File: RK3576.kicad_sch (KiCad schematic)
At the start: 0 parts

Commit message: Add files via upload
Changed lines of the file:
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@@
+		)
+	)
+	(bus
+		(pts
+			(xy 0.1524 0.1524) (xy 53.4924 0.1524)
+		)
+		(stroke
+			(width 0)
+			(type default)
 		)
 	)

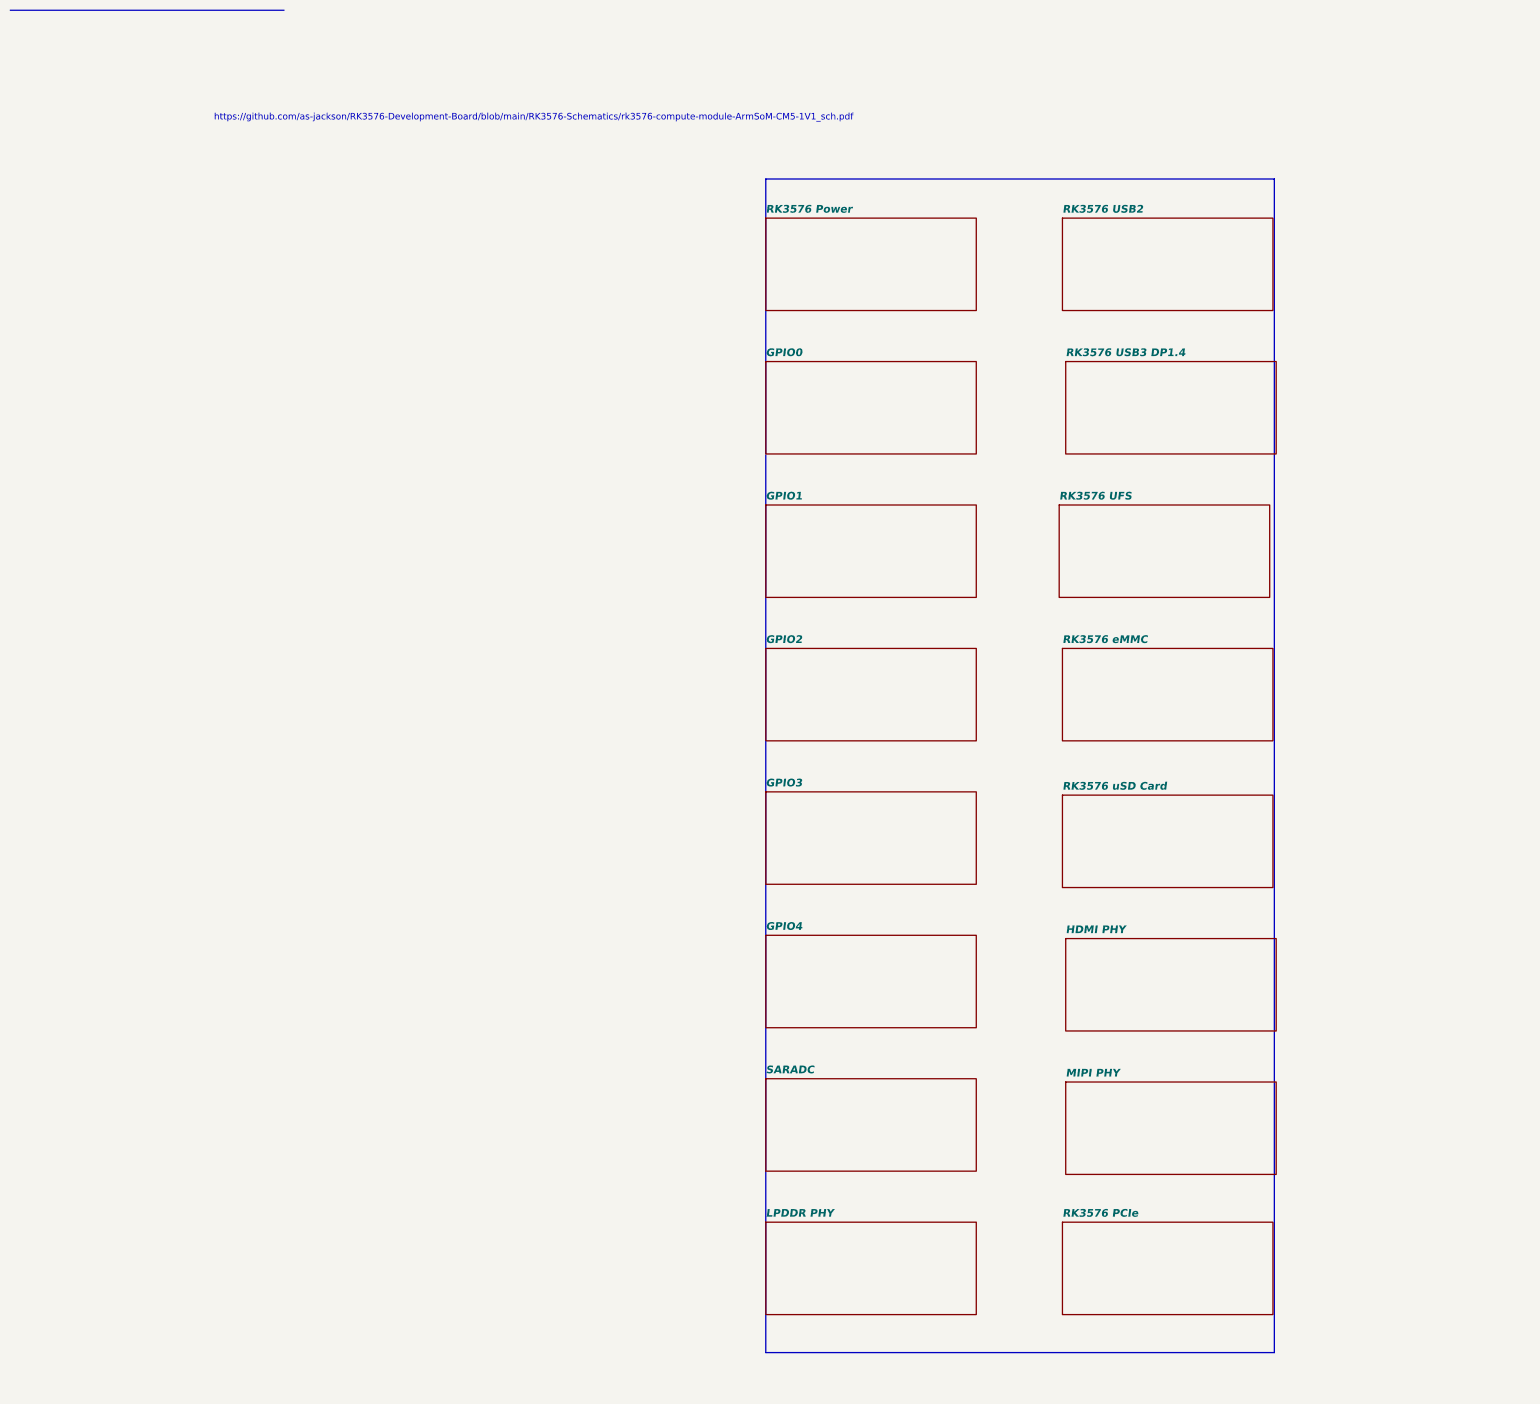
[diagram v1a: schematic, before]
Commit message: SBC Board V0.2
The SBC schematics before footprint and part number check
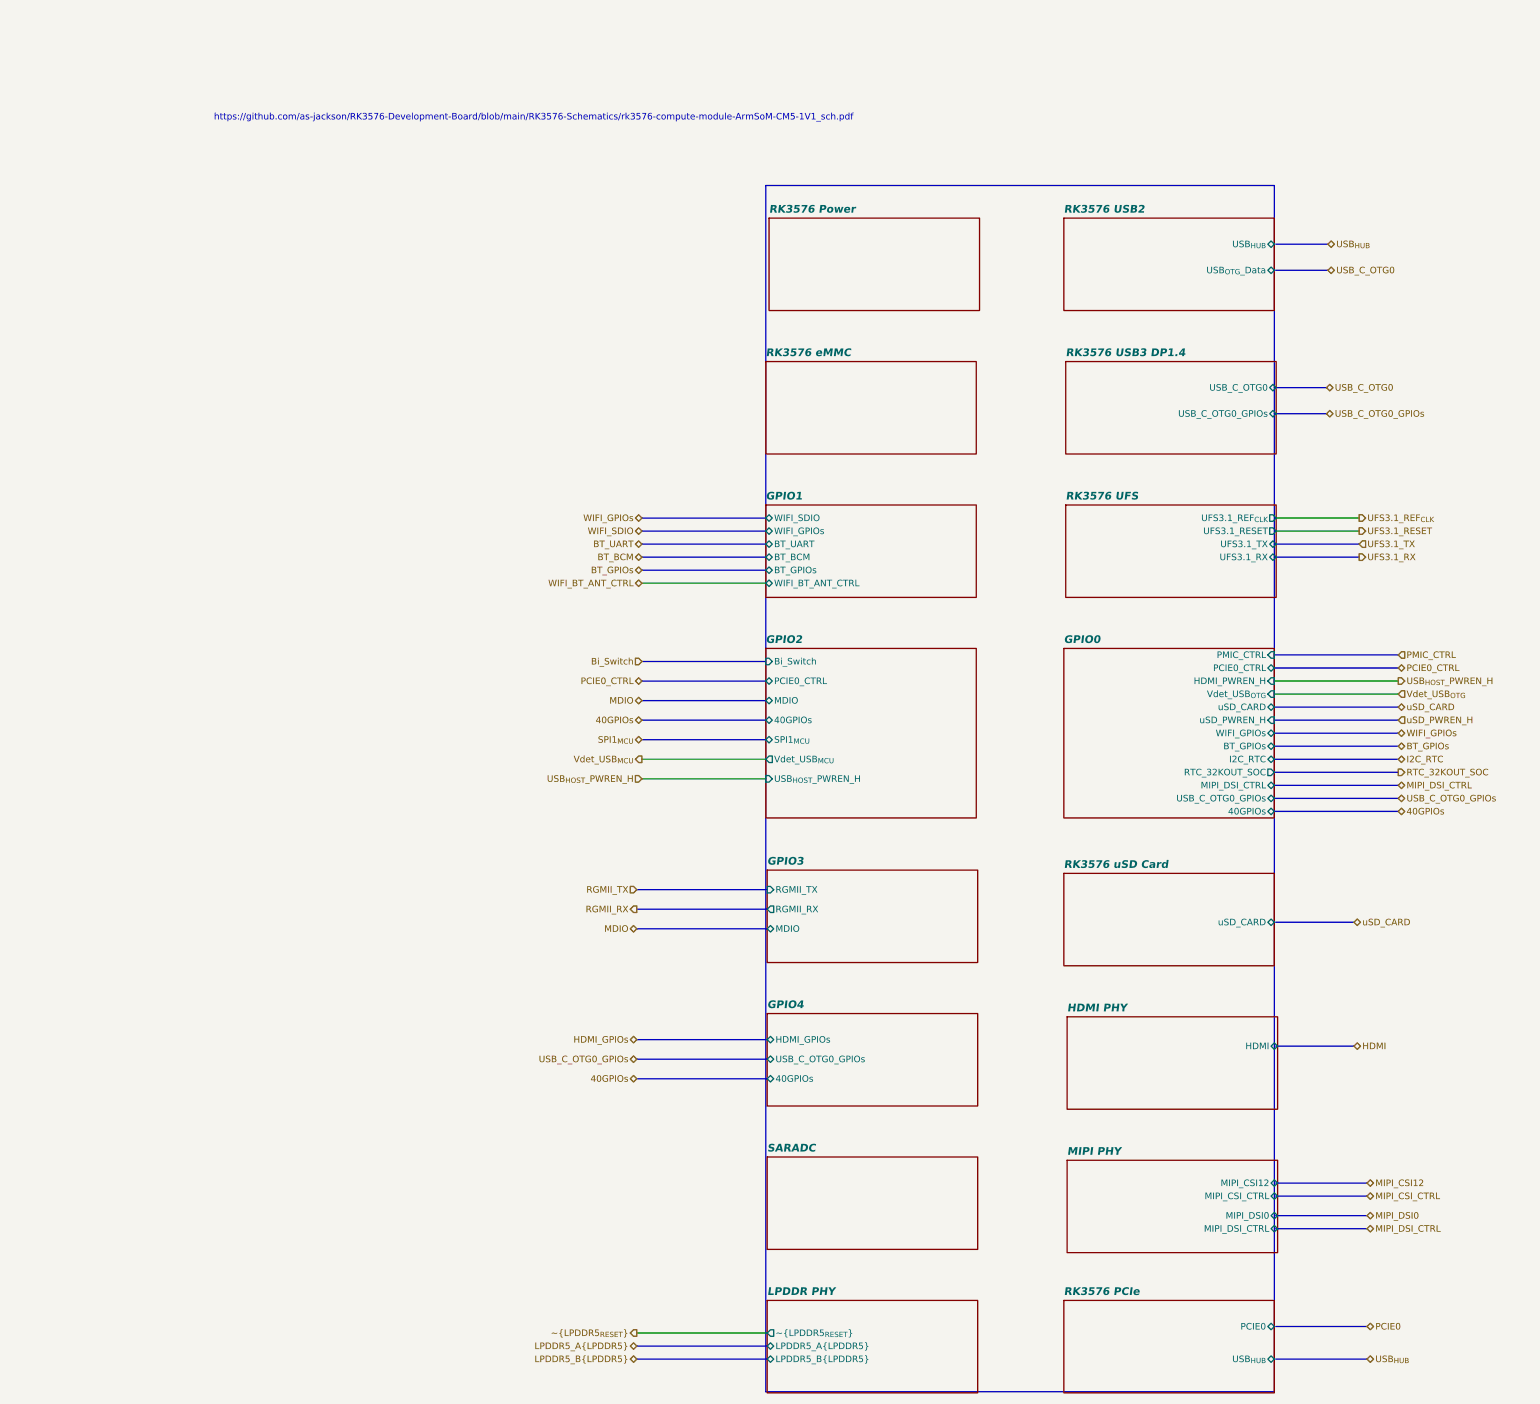
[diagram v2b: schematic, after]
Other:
- sheet GPIO0 ports: added 40GPIOs, BT_GPIOs, HDMI_PWREN_H, I2C_RTC, MIPI_DSI_CTRL, PCIE0_CTRL, PMIC_CTRL, RTC_32KOUT_SOC, USB_C_OTG0_GPIOs, Vdet_USB_{OTG}, WIFI_GPIOs, uSD_CARD, uSD_PWREN_H; removed none
- sheet GPIO1 ports: added BT_BCM, BT_GPIOs, BT_UART, WIFI_BT_ANT_CTRL, WIFI_GPIOs, WIFI_SDIO; removed none
- sheet GPIO2 ports: added 40GPIOs, Bi_Switch, MDIO, PCIE0_CTRL, SPI1_{MCU}, USB_{HOST}_PWREN_H, Vdet_USB_{MCU}; removed none
- sheet GPIO3 ports: added MDIO, RGMII_RX, RGMII_TX; removed none
- sheet GPIO4 ports: added 40GPIOs, HDMI_GPIOs, USB_C_OTG0_GPIOs; removed none
- sheet HDMI PHY ports: added HDMI; removed none
- sheet LPDDR PHY ports: added LPDDR5_A{LPDDR5}, LPDDR5_B{LPDDR5}, ~{LPDDR5_{RESET}}; removed none
- sheet MIPI PHY ports: added MIPI_CSI12, MIPI_CSI_CTRL, MIPI_DSI0, MIPI_DSI_CTRL; removed none
- sheet RK3576 PCIe ports: added PCIE0, USB_{HUB}; removed none
- sheet RK3576 UFS ports: added UFS3.1_REF_{CLK}, UFS3.1_RESET, UFS3.1_RX, UFS3.1_TX; removed none
- sheet RK3576 USB2 ports: added USB_{HUB}, USB_{OTG}_Data; removed none
- sheet RK3576 USB3 DP1.4 ports: added USB_C_OTG0, USB_C_OTG0_GPIOs; removed none
- sheet RK3576 uSD Card ports: added uSD_CARD; removed none

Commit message: Release v2: replace main with RK3576 SBCv2, archive v1 to branch archive/v1
- main now shows only v2 (RK3576 SBCv2.kicad_pro)
- v1 preserved in branch archive/v1 + tag v1.0
- Add .gitignore for KiCad (*.bak, *.lck, .history/)
- Update README with version switcher
- Cleaned: dropped 141M .history, Resources ref PDF, *.bak/*.lck
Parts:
- added C100, C101, C107, C108, C114, C120, C122, C123, C124, C125, C126, C127, C128, C129, C130, C131, C132, C133, C134, C135, C136, C141, C142, C151, C153, C155, C156, C157, C158, C159, C160, C161, C162, C163, C164, C165, C166, C167, C168, C169, C170, C233, C336, C337, C338, C339, C340, C341, C346, C347, C348, C357, C360, C401, C420, C421, C422, C423, C424, C425, C426, C427, C428, C429, C430, C431, C432, C433, C69, C70, C73, C74, C75, C97, C99: 1u, Capacitor_SMD:C_0201_0603Metric_Pad0.64x0.40mm_HandSolder, symbol New_Library_0:C_Small_edited
- added C102, C103, C104, C105, C106, C109, C113, C117, C118, C96: 100n, Capacitor_SMD:C_0201_0603Metric_Pad0.64x0.40mm_HandSolder, symbol New_Library_0:C_Small_edited
- added C110, C111, C115, C116, C152, C154, C67, C76, C98: 10u, Capacitor_SMD:C_0603_1608Metric, symbol New_Library_0:C_Small_edited
- added C119, C121: 12pF, Capacitor_SMD:C_0402_1005Metric_Pad0.74x0.62mm_HandSolder, symbol New_Library_0:C_Small_edited
- added C137, C138, C139, C140, C145, C146, C211, C230, C231, C234, C235, C236, C237, C307: 22u, Capacitor_SMD:C_0603_1608Metric, symbol New_Library_0:C_Small_edited
- added C358, C359: 18pF, Capacitor_SMD:C_0402_1005Metric_Pad0.74x0.62mm_HandSolder, symbol New_Library_0:C_Small_edited
- added D3, D4: PESD5V0S1BA, PCM_Diode_SMD_AKL:D_SOD-323_TVS, symbol PCM_Diode_TVS_AKL:PESD5V0S1BA
- added D6: SMBJ5.0CA, PCM_Diode_SMD_AKL:D_SMB_TVS, symbol PCM_Diode_TVS_AKL:SMBJ5.0CA
- added J21: B4B Connector, Connector:FanPinHeader_1x04_P2.54mm_Vertical, symbol Connector:Conn_01x04_Pin
- added LED1, LED2: XL-1608SURC-06, PCM_LED_SMD_AKL:LED_0603_1608Metric, symbol PCM_LED_AKL:LED_0603_Red
- added Q1: 2SK3018, PCM_Package_TO_SOT_SMD_AKL:SOT-323_SC-70, symbol PCM_Transistor_MOSFET_AKL:2SK3018
- added R145, R146, R17: 1k, PCM_Resistor_SMD_AKL:R_0402_1005Metric, symbol Device:R_Small
- added R148, R258: 510k, PCM_Resistor_SMD_AKL:R_0402_1005Metric, symbol Device:R_Small
- added R18: 100k, PCM_Resistor_SMD_AKL:R_0402_1005Metric, symbol Device:R_Small
- added R19, R20: 100R, PCM_Resistor_SMD_AKL:R_0402_1005Metric, symbol Device:R_Small
- added R225, R264, R265, R266, R267, R282, R283: 10k, PCM_Resistor_SMD_AKL:R_0402_1005Metric, symbol Device:R_Small
- added R227, R228, R231, R232, R259: 22R, PCM_Resistor_SMD_AKL:R_0402_1005Metric, symbol Device:R_Small
- added R229: 0R, PCM_Resistor_SMD_AKL:R_0402_1005Metric, symbol Device:R_Small
- added R233, R239: 4.7k, PCM_Resistor_SMD_AKL:R_0402_1005Metric, symbol Device:R_Small
- added R236, R240: 200R, PCM_Resistor_SMD_AKL:R_0402_1005Metric, symbol Device:R_Small
- added R260, R35, R42: 8.2k, PCM_Resistor_SMD_AKL:R_0402_1005Metric, symbol Device:R_Small
- added R261: 6.8k, PCM_Resistor_SMD_AKL:R_0402_1005Metric, symbol Device:R_Small
- added R262: 23.2k, PCM_Resistor_SMD_AKL:R_0402_1005Metric, symbol Device:R_Small
- added R263: 88.7k, PCM_Resistor_SMD_AKL:R_0402_1005Metric, symbol Device:R_Small
- added SW7: DSHP03TS-S, Button_Switch_SMD:SW_DIP_SPSTx03_Slide_KingTek_DSHP03TJ_W5.25mm_P1.27mm_JPin, symbol Switch:SW_DIP_x03
- added SW9: XUNPU TS-1089S-02526, easyeda2kicad:XUNPU TS-1089S-02526, symbol Switch:SW_Push
- added U12: RK3576, easyeda2kicad:FCCSP-698_L17.2-W16.1-TL_RK3576, symbol RK3576:RK3576
- added Y2: TXM24M0004322FBCDO00T, Crystal:Crystal_SMD_3225-4Pin_3.2x2.5mm, symbol Device:Crystal_GND24
- added Y9: XTM32026000FT00351001, Crystal:Crystal_SMD_3225-4Pin_3.2x2.5mm, symbol Device:Crystal_GND24
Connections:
- net RTC_32KOUT_SOC: now also U12.1U23 (CLK_32K_IN)
- net UFS3.1_REF_{CLK}: now also U12.AK4 (UFS_REFCLK)
- net UFS3.1_RESET: now also U12.1AD2 (UFS_RSTN)
- net USB_{HOST}_PWREN_H: now also U12.1A5 (SAI1_SDO1_M0)
- net Vdet_USB_{MCU}: now also U12.1C12 (VO_LCDC_D3)
- net uSD_PWREN_H: now also U12.1Y24 (SDMMC0_PWREN)
- new net: LED1.2 (A), R145.2
- new net: R232.1, U12.1R6 (ZQ_A)
- new net: C359.1, R259.2, Y9.1
- new net: C358.1, R258.2, U12.AL5 (OSC_UFS_XOUT), Y9.3
- new net: R239.1, U12.2T10 (USB2_OTG1_VBUSDET)
- new net: R236.1, U12.2R3 (USB2_OTG0_REXT)
- new net: R231.1, U12.1J6 (ZQ_B)
- new net: R227.1, U12.2C2 (DDRPHY_PLL_AVSS)
- new net: R240.1, U12.2U8 (USB2_OTG1_REXT)
- new net: C119.1, R228.1, Y2.1
- new net: R263.2, SW7.3
- new net: R262.2, SW7.2
- new net: C121.1, R148.2, U12.U28 (OSC_XIN), Y2.3
- new net: Q1.1 (G), R17.2, R18.1
- new net: LED1.1 (K), Q1.3 (D)
- new net: LED2.2 (A), R146.2
- new net: C168.1, U12.2N7 (MIPI_DCPHY_VREG)
- new net: R19.1, U12.1U24 (UART0_TX_M0)
- new net: R20.1, U12.AA28 (UART0_RX_M0)
- new net: R148.1, R228.2, U12.U29 (OSC_XOUT)
- new net: R233.1, U12.2P3 (USB2_OTG0_VBUSDET)
- new net: R261.2, SW7.1
- new net: R258.1, R259.1, U12.AK5 (OSC_UFS_XIN)
- new net 40GPIOs_GPIO(3_A0)_UART(3)_RX-M1: U12.1B12 (SPDIF_RX0_M1)
- new net 40GPIOs_GPIO(3_A1)_UART(3)_RX-M1: U12.1B7 (VO_POST_EMPTY)
- new net 40GPIOs_GPIO(3_A6)_UART(1)_RX-M2: U12.1A7 (VO_LCDC_D21)
- new net 40GPIOs_GPIO(3_A7)_UART(1)_TX-M2: U12.B13 (VO_LCDC_D20)
- new net 40GPIOs_GPIO(3_B0)_UART(10)_RX-M0: U12.B14 (VO_LCDC_D19)
- new net 40GPIOs_GPIO(3_B1)_UART(10)_TX-M0: U12.1A11 (VO_LCDC_D18)
- new net 40GPIOs_GPIO(3_B2)_I2C(8)_SDA-M3: U12.A13 (VO_LCDC_D17)
- new net 40GPIOs_GPIO(3_B3)_I2C(8)_SCL-M3: U12.A11 (VO_LCDC_D16)
- new net 40GPIOs_GPIO(3_B4)_PWM(1)_CH4-M3: U12.B10 (VO_LCDC_D15)
- new net 40GPIOs_GPIO(3_B5)_PWM(1)_CH5-M3: U12.1A9 (VO_LCDC_D14)
- new net 40GPIOs_GPIO(3_B6)_PWM(0)_CH1-M3: U12.B11 (VO_LCDC_D13)
- new net 40GPIOs_GPIO(3_B7)_UART(2)_RX-M2: U12.1D12 (VO_LCDC_D12)
- new net 40GPIOs_GPIO(3_C0)_UART(2)_TX-M2: U12.1E9 (VO_LCDC_D11)
- new net 40GPIOs_GPIO(3_C1)_I2C(5)_SDA-M3: U12.1B10 (VO_LCDC_D10)
- new net 40GPIOs_GPIO(3_C2)_I2C(5)_SCL-M3: U12.B9 (VO_LCDC_D9)
- new net 40GPIOs_GPIO(3_C3)_I2C(9)_SDA-M3: U12.1A8 (VO_LCDC_D8)
- new net 40GPIOs_GPIO(3_C4)_I2C(9)_SCL-M3: U12.1D9 (VO_LCDC_D7)
- new net 40GPIOs_GPIO(3_C5)_PWM(2)_CH2-M3: U12.1B9 (VO_LCDC_D6)
- new net 40GPIOs_GPIO(3_C6): U12.1D7 (VO_LCDC_D5)
- new net 40GPIOs_GPIO(3_C7): U12.1C7 (VO_LCDC_D4)
- new net 40GPIOs_GPIO(3_D1)_I3C(1)_SDA_PU-M2: U12.1A12 (VO_LCDC_D2)
- new net 40GPIOs_GPIO(3_D2)_I3C(1)_SDA-M2: U12.1A10 (VO_LCDC_D1)
- new net 40GPIOs_GPIO(3_D3)_I3C(1)_SCL-M2: U12.B12 (VO_LCDC_D0)
- new net 40GPIOs_PWR_EN: U12.AD28 (REF_CLK1_OUT)
- new net BT_REG_ON_L: U12.1W21 (PDM0_CLK1_M0)
- new net BT_WAKE_DEV_L: U12.1C22 (ETH1_RXD0_M1)
- new net BT_WAKE_HOST_L: U12.A26 (ETH1_TXCTL_M1)
- new net CSI0_RX_CLK_N: U12.AL22 (MIPI_DPHY_CSI0_RX_CLKN)
- new net CSI0_RX_CLK_P: U12.AK22 (MIPI_DPHY_CSI0_RX_CLKP)
- new net CSI0_RX_D0_N: U12.AL20 (MIPI_DPHY_CSI0_RX_D0N)
- new net CSI0_RX_D0_P: U12.AK20 (MIPI_DPHY_CSI0_RX_D0P)
- new net CSI0_RX_D1_N: U12.AL21 (MIPI_DPHY_CSI0_RX_D1N)
- new net CSI0_RX_D1_P: U12.AK21 (MIPI_DPHY_CSI0_RX_D1P)
- new net CSI0_RX_D2_N: U12.AL23 (MIPI_DPHY_CSI0_RX_D2N)
- new net CSI0_RX_D2_P: U12.AK23 (MIPI_DPHY_CSI0_RX_D2P)
- new net CSI0_RX_D3_N: U12.AL24 (MIPI_DPHY_CSI0_RX_D3N)
- new net CSI0_RX_D3_P: U12.AK24 (MIPI_DPHY_CSI0_RX_D3P)
- new net DSI0_TX_CLK_N: U12.AK17 (MIPI_DPHY_DSI_TX_CLKN)
- new net DSI0_TX_CLK_P: U12.AL17 (MIPI_DPHY_DSI_TX_CLKP)
- new net DSI0_TX_D0_N: U12.AK15 (MIPI_DPHY_DSI_TX_D0N)
- new net DSI0_TX_D0_P: U12.AL15 (MIPI_DPHY_DSI_TX_D0P)
- new net DSI0_TX_D1_N: U12.AK16 (MIPI_DPHY_DSI_TX_D1N)
- new net DSI0_TX_D1_P: U12.AL16 (MIPI_DPHY_DSI_TX_D1P)
- new net DSI0_TX_D2_N: U12.AK18 (MIPI_DPHY_DSI_TX_D2N)
- new net DSI0_TX_D2_P: U12.AL18 (MIPI_DPHY_DSI_TX_D2P)
- new net DSI0_TX_D3_N: U12.AK19 (MIPI_DPHY_DSI_TX_D3N)
- new net DSI0_TX_D3_P: U12.AL19 (MIPI_DPHY_DSI_TX_D3P)
- new net EEPROM_WP: U12.1D13 (VO_LCDC_D23)
- new net ETH0_{PHY}_CLK_{OUT}: U12.1E15 (CAM_CLK2_OUT_M1)
- new net ETH0_{PHY}_INT: U12.1C6 (SAI1_SCLK_M0)
- new net ETH0_{PHY}_MDC: U12.1B18 (VI_CIF_VSYNC)
- new net ETH0_{PHY}_MDIO: U12.1D16 (VI_CIF_HREF)
- new net ETH0_{PHY}_RESET: U12.1D6 (SAI1_MCLK_M0)
- new net ETH0_{PHY}_RXC: U12.1C18 (VI_CIF_D8)
- new net ETH0_{PHY}_RXCTL: U12.1A20 (VI_CIF_CLKO)
- new net ETH0_{PHY}_RXD0: U12.B22 (VI_CIF_D15)
- new net ETH0_{PHY}_RXD1: U12.1A19 (VI_CIF_CLKI)
- new net ETH0_{PHY}_RXD2: U12.B21 (VI_CIF_D6)
- new net ETH0_{PHY}_RXD3: U12.A21 (VI_CIF_D7)
- new net ETH0_{PHY}_TXC: U12.1B16 (VI_CIF_D10)
- new net ETH0_{PHY}_TXCTL: U12.B20 (VI_CIF_D14)
- new net ETH0_{PHY}_TXD0: U12.1A18 (VI_CIF_D12)
- new net ETH0_{PHY}_TXD1: U12.B19 (VI_CIF_D13)
- new net ETH0_{PHY}_TXD2: U12.A19 (VI_CIF_D9)
- new net ETH0_{PHY}_TXD3: U12.1A17 (VI_CIF_D11)
- new net ETH1_{PHY}_CLK_{OUT}: U12.1D18 (CAM_CLK1_OUT_M1)
- new net ETH1_{PHY}_INT: U12.1B6 (SAI1_LRCK_M0)
- new net ETH1_{PHY}_MDC: U12.1B13 (ISP_PRELIGHT_TRIG_M0)
- new net ETH1_{PHY}_MDIO: U12.1B15 (ISP_FLASH_TRIGOUT_M0)
- new net ETH1_{PHY}_RESET: U12.1C5 (SAI4_SCLK_M0)
- new net ETH1_{PHY}_RXC: U12.1D15 (VI_CIF_D3)
- new net ETH1_{PHY}_RXCTL: U12.B18 (ETH1_RXCTL_M0)
- new net ETH1_{PHY}_RXD0: U12.1A16 (ETH1_RXD0_M0)
- new net ETH1_{PHY}_RXD1: U12.B17 (CAM_CLK0_OUT_M1)
- new net ETH1_{PHY}_RXD2: U12.A17 (VI_CIF_D5)
- new net ETH1_{PHY}_RXD3: U12.1A15 (VI_CIF_D4)
- new net ETH1_{PHY}_TXC: U12.1C15 (VI_CIF_D0)
- new net ETH1_{PHY}_TXCTL: U12.B16 (ETH1_TXCTL_M0)
- new net ETH1_{PHY}_TXD0: U12.1A14 (ETH1_TXD0_M0)
- new net ETH1_{PHY}_TXD1: U12.B15 (ETH1_TXD1_M0)
- new net ETH1_{PHY}_TXD2: U12.A15 (VI_CIF_D2)
- new net ETH1_{PHY}_TXD3: U12.1A13 (VI_CIF_D1)
- new net FSPI0_CLE/EMMC_DATA_STROBE: U12.1F23 (EMMC_STRB)
- new net FSPI0_CMD/EMMC_CMD: U12.1F22 (EMMC_CMD)
- new net FSPI0_D0/EMMC_D0: U12.E28 (EMMC_D0)
- new net FSPI0_D1/EMMC_D1: U12.E29 (EMMC_D1)
- new net FSPI0_D2/EMMC_D2: U12.1C24 (EMMC_D2)
- new net FSPI0_D3/EMMC_D3: U12.F28 (EMMC_D3)
- new net FSPI0_D4/EMMC_D4: U12.1D24 (EMMC_D4)
- new net FSPI0_D5/EMMC_D5: U12.G28 (EMMC_D5)
- new net FSPI0_D6/EMMC_D6: U12.D28 (EMMC_D6)
- new net FSPI0_D7/EMMC_D7: U12.1B24 (EMMC_D7)
- new net FSPI0_DS/EMMC_CLK_OUT: U12.1G23 (EMMC_CLK)
- new net FSPI0_WPn/EMMC_Reset: U12.1D23 (EMMC_RSTN)
- new net GND: C100.2, C101.2, C102.2, C103.2, C104.2, C105.2, C106.2, C107.2, C108.2, C109.2, C110.2, C111.2, C113.2, C114.2, C115.2, C116.2, C117.2, C118.2, C119.2, C120.2, C121.2, C122.2, C123.2, C124.2, C125.2, C126.2, C127.2, C128.2, C129.2, C130.2, C131.2, C132.2, C133.2, C134.2, C135.2, C136.2, C137.2, C138.2, C139.2, C140.2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
- new net HDMI_CK_N: U12.AK26 (HDMI_TX_D3N)
- new net HDMI_CK_P: U12.AL26 (HDMI_TX_D3P)
- new net HDMI_D0_N: U12.AK27 (HDMI_TX_D0N)
- new net HDMI_D0_P: U12.1AE24 (HDMI_TX_D0P)
- new net HDMI_D1_N: U12.AL28 (HDMI_TX_D1N)
- new net HDMI_D1_P: U12.AK28 (HDMI_TX_D1P)
- new net HDMI_D2_N: U12.AK29 (HDMI_TX_D2N)
- new net HDMI_D2_P: U12.AJ28 (HDMI_TX_D2P)
- new net HDMI_PWREN_H: U12.AK1 (ISP_FLASH_TRIGOUT_M1)
- new net HDMI_REXT: R42.1, U12.1AA20 (HDMI_TX_REXT)
- new net HDMI_TX_CEC_M0: U12.AK3 (DSM_AUD_LP_M1)
- new net HDMI_TX_EDP_TX_AVDDD0V75: C152.1, C153.1, U12.2N11 (HDMI_TX_EDP_TX_AVDDD0V75), U12.2P11 (HDMI_TX_EDP_TX_AVDDC0V75)
- new net HDMI_TX_EDP_TX_AVDDIO1V8: C141.1, C154.1, C155.1, C157.1, C163.1, C166.1, C167.1, C170.1, C338.1, C339.1, C341.1, C348.1, C357.1, C360.1, C401.1, C420.1, R264.1, R265.1, R266.1, R282.1, U12.1J20 (VCCIO0_VCC1V8), U12.1W20 (MIPI_DPHY_CSI1/2_RX_AVDD1V8), U12.2A10 (SARADC_AVDD1V8), U12.2D12 (MIPI_DPHY_CSI3/4_RX_AVDD1V8), U12.2D2 (DDRPHY_PLL_AVDD1V8), U12.2E12 (PCIE1_SATA1_USB3_OTG1_AVDD1V8), U12.2F12 (PCIE0_SATA0_AVDD1V8), U12.2M2 (OSC_UFS_AVDD), U12.2N10 (HDMI_TX_EDP_TX_AVDDIO1V8), U12.2N4 (USB3_OTG0_DP_TX_AVDD1V8), U12.2P10 (HDMI_TX_EDP_TX_AVDDCMN1V8), U12.2P2 (UFS_AVDD1V8), U12.2P4 (USB2_OTG_AVDD1V8), U12.2P8 (MIPI_DCPHY_AVDD1V8)
- new net HDMI_TX_HPDIN_M0: U12.AK2 (DSM_AUD_LN_M1)
- new net HDMI_TX_ON: U12.AL3 (ISP_PRELIGHT_TRIG_M1)
- new net HDMI_TX_SBD_N: U12.2U12 (HDMI_TX_SBDN)
- new net HDMI_TX_SBD_P: U12.2T12 (HDMI_TX_SBDP)
- new net HDMI_TX_SCL: U12.AL2 (DSM_AUD_RP_M1)
- new net HDMI_TX_SDA: U12.1AE2 (DSM_AUD_RN_M1)
- new net I2C0_SCL_M1_TP_Wireless: U12.1V24 (I2C0_SDA_M1)
- new net I2C0_SDA_M1_TP_Wireless: U12.AB28 (I2C0_SCL_M1)
- new net I2C1_SCL_M0_RK806: U12.1T22 (SPI2_CLK_M0)
- new net I2C1_SDA_M0_RK806: U12.1T23 (SPI2_MOSI_M0)
- new net I2C2_SCL_M0_CC_RTC_EEPROM: U12.1W24 (I2C2_SCL_M0)
- new net I2C2_SDA_M0_CC_RTC_EEPROM: U12.AB29 (I2C2_SDA_M0)
- new net JTAG_TCK_M1 & UART0_TX_M0: J21.2 (Pin_2), R19.2
- new net JTAG_TMS_M1 & UART0_RX_M0: D3.2 (A), D4.2 (A), J21.3 (Pin_3), R20.2
- new net LCD_BL_PWM1_CH1_M0: U12.AD29 (REF_CLK2_OUT)
- new net LCD_PWREN_H: U12.1W23 (SAI0_SDI0_M1)
- new net LCD_RST_L: U12.AC28 (SAI0_SDI1_M1)
- new net LPDDR5_A.CA0: U12.T1 (LP4_A0_A)
- new net LPDDR5_A.CA1: U12.1N1 (LP4_A1_A)
- new net LPDDR5_A.CA2: U12.1R3 (LP4_A2_A)
- new net LPDDR5_A.CA3: U12.1T2 (LP4_A3_A)
- new net LPDDR5_A.CA4: U12.1M5 (LP4_A4_A)
- new net LPDDR5_A.CA5: U12.1P5 (LP4_A5_A)
- new net LPDDR5_A.CA6: U12.1R5 (LP5_A6_A)
- new net LPDDR5_A.CK_N: U12.P1 (LP4_CLKN_A)
- new net LPDDR5_A.CK_P: U12.1L1 (LP4_CLKP_A)
- new net LPDDR5_A.CS0: U12.1N3 (LP4_CKE0_A)
- new net LPDDR5_A.CS1: U12.1N5 (LP4_CKE1_A)
- new net LPDDR5_A.DMI0: U12.1V1 (LP4_DMI0_A)
- new net LPDDR5_A.DMI1: U12.AE1 (LP4_DMI1_A)
- new net LPDDR5_A.DQ0: U12.W1 (LP4_DQ0_A)
- new net LPDDR5_A.DQ1: U12.1T1 (LP4_DQ1_A)
- new net LPDDR5_A.DQ10: U12.1AD1 (LP4_DQ10_A)
- new net LPDDR5_A.DQ11: U12.AH1 (LP4_DQ11_A)
- new net LPDDR5_A.DQ12: U12.1Y1 (LP4_DQ12_A)
- new net LPDDR5_A.DQ13: U12.1W2 (LP4_DQ13_A)
- new net LPDDR5_A.DQ14: U12.1AA3 (LP4_DQ14_A)
- new net LPDDR5_A.DQ15: U12.1AA1 (LP4_DQ15_A)
- new net LPDDR5_A.DQ2: U12.1P1 (LP4_DQ2_A)
- new net LPDDR5_A.DQ3: U12.U1 (LP4_DQ3_A)
- new net LPDDR5_A.DQ4: U12.1V3 (LP4_DQ4_A)
- new net LPDDR5_A.DQ5: U12.1W4 (LP4_DQ5_A)
- new net LPDDR5_A.DQ6: U12.AC1 (LP4_DQ6_A)
- new net LPDDR5_A.DQ7: U12.AB1 (LP4_DQ7_A)
- new net LPDDR5_A.DQ8: U12.AF1 (LP4_DQ8_A)
- new net LPDDR5_A.DQ9: U12.1AB1 (LP4_DQ9_A)
- new net LPDDR5_A.RDQS0_N: U12.Y1 (LP4_DQS0N_A)
- new net LPDDR5_A.RDQS0_P: U12.1U1 (LP4_DQS0P_A)
- new net LPDDR5_A.RDQS1_N: U12.1AB3 (LP4_DQS1N_A)
- new net LPDDR5_A.RDQS1_P: U12.1AB4 (LP4_DQS1P_A)
- new net LPDDR5_A.WCK0_N: U12.1V4 (LP5_WCK0N_A)
- new net LPDDR5_A.WCK0_P: U12.1V5 (LP5_WCK0P_A)
- new net LPDDR5_A.WCK1_N: U12.1AA5 (LP5_WCK1N_A)
- new net LPDDR5_A.WCK1_P: U12.1AA6 (LP5_WCK1P_A)
- new net LPDDR5_B.CA0: U12.L1 (LP4_A0_B)
- new net LPDDR5_B.CA1: U12.1J1 (LP4_A1_B)
- new net LPDDR5_B.CA2: U12.1J3 (LP4_A2_B)
- new net LPDDR5_B.CA3: U12.1G2 (LP4_A3_B)
- new net LPDDR5_B.CA4: U12.1F4 (LP4_A4_B)
- new net LPDDR5_B.CA5: U12.1K5 (LP4_A5_B)
- new net LPDDR5_B.CA6: U12.1H5 (LP5_A6_B)
- new net LPDDR5_B.CK_N: U12.N1 (LP4_CLKN_B)
- new net LPDDR5_B.CK_P: U12.1K1 (LP4_CLKP_B)
- new net LPDDR5_B.CS0: U12.1K2 (LP4_CKE0_B)
- new net LPDDR5_B.CS1: U12.1M3 (LP4_CKE1_B)
- new net LPDDR5_B.DMI0: U12.B4 (LP4_DMI0_B)
- new net LPDDR5_B.DMI1: U12.1B1 (LP4_DMI1_B)
- new net LPDDR5_B.DQ0: U12.1D2 (LP4_DQ0_B)
- new net LPDDR5_B.DQ1: U12.1F2 (LP4_DQ1_B)
- new net LPDDR5_B.DQ10: U12.B2 (LP4_DQ10_B)
- new net LPDDR5_B.DQ11: U12.A2 (LP4_DQ11_B)
- new net LPDDR5_B.DQ12: U12.1E1 (LP4_DQ12_B)
- new net LPDDR5_B.DQ13: U12.1C1 (LP4_DQ13_B)
- new net LPDDR5_B.DQ14: U12.E1 (LP4_DQ14_B)
- new net LPDDR5_B.DQ15: U12.D1 (LP4_DQ15_B)
- new net LPDDR5_B.DQ2: U12.1G1 (LP4_DQ2_B)
- new net LPDDR5_B.DQ3: U12.K1 (LP4_DQ3_B)
- new net LPDDR5_B.DQ4: U12.1C3 (LP4_DQ4_B)
- new net LPDDR5_B.DQ5: U12.1B3 (LP4_DQ5_B)
- new net LPDDR5_B.DQ6: U12.A5 (LP4_DQ6_B)
- new net LPDDR5_B.DQ7: U12.G1 (LP4_DQ7_B)
- new net LPDDR5_B.DQ8: U12.1A1 (LP4_DQ8_B)
- new net LPDDR5_B.DQ9: U12.B1 (LP4_DQ9_B)
- new net LPDDR5_B.RDQS0_N: U12.1F1 (LP4_DQS0N_B)
- new net LPDDR5_B.RDQS0_P: U12.H1 (LP4_DQS0P_B)
- new net LPDDR5_B.RDQS1_N: U12.B3 (LP4_DQS1N_B)
- new net LPDDR5_B.RDQS1_P: U12.A3 (LP4_DQS1P_B)
- new net LPDDR5_B.WCK0_N: U12.1G4 (LP5_WCK0N_B)
- new net LPDDR5_B.WCK0_P: U12.1G5 (LP5_WCK0P_B)
- new net LPDDR5_B.WCK1_N: U12.1E4 (LP5_WCK1N_B)
- new net LPDDR5_B.WCK1_P: U12.1D4 (LP5_WCK1P_B)
- new net LPDDR5_RESET: U12.1U5 (LP4_RESET)
- new net PCIE0_CLKREQ_L: U12.1A6 (SAI1_SDI0_M0)
- new net PCIE0_DET_L: U12.1A4 (SPDIF_TX0_M0)
- new net PCIE0_REFCLK_N: U12.1N23 (PCIE0_REFCLKN)
- new net PCIE0_REFCLK_P: U12.1N22 (PCIE0_REFCLKP)
- new net PCIE0_RESET_L: U12.B6 (SAI1_SDO3_M0)
- new net PCIE0_RX_N: U12.R29 (PCIE0_RXN)
- new net PCIE0_RX_P: U12.R28 (PCIE0_RXP)
- new net PCIE0_TX_N: U12.P28 (PCIE0_TXN)
- new net PCIE0_TX_P: U12.P29 (PCIE0_TXP)
- new net PCIE0_WAKE_L: U12.B8 (SPDIF_RX0_M0)
- new net PMIC_INT_L: U12.1T21 (PMIC_INT)
- new net PMIC_PWR_CTRL1: U12.Y28 (PWR_CTRL1)
- new net PMIC_PWR_CTRL2: U12.1T24 (PWR_CTRL2)
- new net PMIC_PWR_CTRL3: U12.Y29 (PWR_CTRL3)
- new net RESET_L: C124.1, R225.2, R229.1, U12.W28 (NPOR)
- new net RTC_INT_L: U12.A9 (VO_LCDC_D22)
- new net SAI2_LRCK_M0: U12.1A24 (ETH1_MDC_M1)
- new net SAI2_SCLK_M0: U12.1D22 (ETH1_RXCTL_M1)
- new net SAI2_SDI_M0: U12.C28 (ETH1_MDIO_M1)
- new net SAI2_SDO_M0: U12.C29 (ETH1_RXD1_M1)
- new net SARADC_VIN0_BOOT: C424.1, R264.2, SW7.4, SW7.5, SW7.6, U12.A25 (SARADC_IN0_BOOT)
- new net SARADC_VIN1_KEY/RECOVERY: C425.1, D6.2 (A), R265.2, SW9.2, U12.1A22 (SARADC_IN1)
- new net SARADC_VIN2_HW_ID: C426.1, R282.2, R283.1, U12.1B19 (SARADC_IN2)
- new net SARADC_VIN3_HP_HOOK: C427.1, U12.1C19 (SARADC_IN3)
- new net SARADC_VIN4_IN: C428.1, U12.1E18 (SARADC_IN4)
- new net SARADC_VIN5_BOM_ID: C429.1, R266.2, R267.1, U12.1D19 (SARADC_IN5)
- new net SARADC_VIN6: C430.1, U12.1D21 (SARADC_IN6)
- new net SARADC_VIN7_DC: C431.1, U12.1E19 (SARADC_IN7)
- new net SDMMC1_CLK_M0: U12.1B22 (ETH1_TXCLK_M1)
- new net SDMMC1_CMD_M0: U12.B26 (ETH1_TXD3_M1)
- new net SDMMC1_D0_M0: U12.A28 (ETH1_RXD2_M1)
- new net SDMMC1_D1_M0: U12.B27 (ETH1_RXD3_M1)
- new net SDMMC1_D2_M0: U12.1A23 (ETH1_RXCLK_M1)
- new net SDMMC1_D3_M0: U12.A27 (ETH1_TXD2_M1)
- new net SPI1_{MCU}_CS: U12.1E7 (VO_LCDC_CLK)
- new net SPI1_{MCU}_SCK: U12.1E12 (VO_LCDC_DEN)
- new net SPI1_{MCU}_SDI: U12.1C10 (VO_LCDC_VSYNC)
- new net SPI1_{MCU}_SDO: U12.1D10 (VO_LCDC_HSYNC)
- new net TP_INT_L: U12.1Y23 (SAI0_LRCK_M1)
- new net TP_RST_L: U12.1Y22 (SAI0_SDI2_M1)
- new net TSADC_CTRL_M0: R229.2, U12.1R24 (TSADC_CTRL_M0)
- new net UART4_CTSN_M1: U12.B29 (ETH1_PPSCLK_M1)
- new net UART4_RTSN_M1: U12.1C23 (ETH1_PPSTRIG_M1)
- new net UART4_RX_M1: U12.1B23 (ETH1_TXD0_M1)
- new net UART4_TX_M1: U12.B28 (ETH1_TXD1_M1)
- new net UFS3.1_RX0_N: U12.AL7 (UFS_RX_D0N)
- new net UFS3.1_RX0_P: U12.AK8 (UFS_RX_D0P)
- new net UFS3.1_RX1_N: U12.AL6 (UFS_RX_D1N)
- new net UFS3.1_RX1_P: U12.AK7 (UFS_RX_D1P)
- new net UFS3.1_TX0_N: U12.1AC6 (UFS_TX_D0N)
- new net UFS3.1_TX0_P: U12.1AD6 (UFS_TX_D0P)
- new net UFS3.1_TX1_N: U12.1AD5 (UFS_TX_D1N)
- new net UFS3.1_TX1_P: U12.1AD4 (UFS_TX_D1P)
- new net UFS3.1_TX_REXT: R260.1, U12.2R2 (UFS_TX_REXT)
- new net USB_{HUB}_D_N: U12.2T5 (USB2_OTG1_DM)
- new net USB_{HUB}_D_P: U12.2T4 (USB2_OTG1_DP)
- new net USB_{HUB}_SSRX1_N: U12.M29 (PCIE1_RXN)
- new net USB_{HUB}_SSRX1_P: U12.M28 (PCIE1_RXP)
- new net USB_{HUB}_SSTX1_N: U12.N29 (PCIE1_TXN)
- new net USB_{HUB}_SSTX1_P: U12.N28 (PCIE1_TXP)
- new net USB_{SOC}_AUX_N: U12.2T3 (DP_TX_AUXN)
- new net USB_{SOC}_AUX_P: U12.2T2 (DP_TX_AUXP)
- new net USB_{SOC}_CON_INT: U12.B7 (SAI1_SDO2_M0)
- new net USB_{SOC}_D_N: U12.AL9 (USB2_OTG0_DM)
- new net USB_{SOC}_D_P: U12.AK9 (USB2_OTG0_DP)
- new net USB_{SOC}_PUPDCTRL1: U12.1B5 (SAI4_LRCK_M0)
- new net USB_{SOC}_PUPDCTRL2: U12.A7 (SAI1_SDO0_M0)
- new net USB_{SOC}_PWREN_H: U12.AJ1 (SAI4_SCLK_M2)
- new net USB_{SOC}_REXT: R35.1, U12.2T7 (USB3_OTG0_REXT)
- new net USB_{SOC}_RX1_N: U12.AL10 (USB3_OTG0_SSRX1N)
- new net USB_{SOC}_RX1_P: U12.AK10 (USB3_OTG0_SSRX1P)
- new net USB_{SOC}_RX2_N: U12.AL12 (USB3_OTG0_SSRX2N)
- new net USB_{SOC}_RX2_P: U12.AK12 (USB3_OTG0_SSRX2P)
- new net USB_{SOC}_TX1_N: U12.AK11 (USB3_OTG0_SSTX1N)
- new net USB_{SOC}_TX1_P: U12.AL11 (USB3_OTG0_SSTX1P)
- new net USB_{SOC}_TX2_N: U12.AK13 (USB3_OTG0_SSTX2N)
- new net USB_{SOC}_TX2_P: U12.AL13 (USB3_OTG0_SSTX2P)
- new net USER_LED: R17.1, U12.1AA23 (SAI0_SDI3_M1)
- new net VCC5V0_SYS: R145.1, R146.1
- new net VCCA_1.8v_S0: C120.1, C125.1, C97.1, U12.2H12 (PLL_AVDD1V8), U12.2J10 (OSC_AVDD1V8), U12.2K11 (PMUIO0_VCC1V8)
- new net VCCA_1V8_S3: C130.1, U12.2B10 (VCCIO3_VCC)
- new net VCC_1.8v_S3: R225.1
- new net VCC_3.3v_S0: C123.1, C129.1, C132.1, C421.1, C422.1, C432.1, C433.1, J21.1 (Pin_1), U12.1U20 (PMUIO1_VCC), U12.2A2 (VCCIO2_VCC), U12.2A4 (VCCIO5_VCC[2]), U12.2A5 (VCCIO5_VCC[2]), U12.2A7 (VCCIO4_VCC), U12.2A8 (VCCIO1_VCC), U12.2N3 (VCCIO6_VCC)
- new net VCC_3V3_S0: C233.1, R233.2, R239.2, U12.2P7 (USB2_OTG_AVDD3V3)
- new net VDD2_DDR_S3: C151.1, U12.2B2 (DDRPHY_CKE_VDDQ)
- new net VDDA_0.75v_S0: C122.1, U12.2G11 (PLL_DVDD0V75)
- new net VDDA_0V75_S0: C158.1, C159.1, C161.1, C162.1, C164.1, C165.1, C169.1, C423.1, U12.2D11 (MIPI_DPHY_CSI3/4_RX_AVDD0V75), U12.2H11 (OTP_DVDD0V75), U12.2L11 (MIPI_DPHY_CSI1/2_RX_AVDD0V75), U12.2M7 (MIPI_DCPHY_AVDD), U12.2P5 (USB2_OTG_DVDD0V75)
- new net VDDA_0V85_S0: C156.1, C336.1, C337.1, C346.1, C347.1, U12.2E11 (PCIE1_SATA1_USB3_OTG1_AVDD0V85), U12.2F11 (PCIE0_SATA0_AVDD0V85), U12.2M5 (USB3_OTG0_DP_TX_AVDD0V85), U12.2N2 (UFS_AVDD0V85), U12.2N5 (USB3_OTG0_DP_TX_DVDD0V85)
- new net VDDA_1V2_S0: C160.1, C340.1, U12.2M3 (VCCIO7_VCC), U12.2M8 (MIPI_DCPHY_AVDD1V2)
- new net VDDA_DDR_PLL_S0: C142.1, U12.2C3 (DDRPHY_PLL_DVDD)
- new net VDDQ_DDR_S0: C128.1, C131.1, C133.1, C137.1, C139.1, C145.1, R231.2, R232.2, U12.2D1 (DDRPHY_CK_VDDQ), U12.2E1 (DDRPHY_VDDQ[6]), U12.2F1 (DDRPHY_VDDQ[6]), U12.2F2 (DDRPHY_VDDQ[6]), U12.2G1 (DDRPHY_VDDQ[6]), U12.2H1 (DDRPHY_VDDQ[6]), U12.2J2 (DDRPHY_VDDQ[6])
- new net VDD_3.3v_S3: C126.1, C127.1, U12.2L10 (PMU_LOGIC_DVDD0V75[2]), U12.2L2 (PMU_LOGIC_DVDD0V75[2])
- new net VDD_CPU_BIG_S0: C100.1, C101.1, C102.1, C103.1, C230.1, C98.1, C99.1, U12.2G5 (CPU_BIG_DVDD[8]), U12.2G6 (CPU_BIG_DVDD[8]), U12.2H6 (CPU_BIG_DVDD[8]), U12.2H7 (CPU_BIG_DVDD[8]), U12.2J6 (CPU_BIG_DVDD[8]), U12.2J7 (CPU_BIG_DVDD[8]), U12.2K6 (CPU_BIG_DVDD[8]), U12.2K7 (CPU_BIG_DVDD[8])
- new net VDD_CPU_LIT_S0: C211.1, C231.1, C67.1, C69.1, C70.1, C96.1, U12.2H4 (CPU_LIT_DVDD[5]), U12.2J3 (CPU_LIT_DVDD[5]), U12.2J4 (CPU_LIT_DVDD[5]), U12.2K3 (CPU_LIT_DVDD[5]), U12.2K4 (CPU_LIT_DVDD[5])
- new net VDD_DDR_S0: C134.1, C135.1, C136.1, C138.1, C140.1, C146.1, U12.2E2 (DDRPHY_DVDD[5]), U12.2F3 (DDRPHY_DVDD[5]), U12.2G2 (DDRPHY_DVDD[5]), U12.2G3 (DDRPHY_DVDD[5]), U12.2H2 (DDRPHY_DVDD[5])
- new net VDD_GPU_S0: C109.1, C113.1, C114.1, C115.1, C116.1, C237.1, U12.2C4 (GPU_DVDD[5]), U12.2C5 (GPU_DVDD[5]), U12.2D4 (GPU_DVDD[5]), U12.2D5 (GPU_DVDD[5]), U12.2E4 (GPU_DVDD[5])
- new net VDD_LOGIC_S0: C104.1, C105.1, C106.1, C107.1, C108.1, C110.1, C111.1, C234.1, C236.1, C73.1, U12.2E7 (LOGIC_DVDD[7]), U12.2F7 (LOGIC_MEM_DVDD[2]), U12.2F8 (LOGIC_DVDD[7]), U12.2F9 (LOGIC_DVDD[7]), U12.2G8 (LOGIC_DVDD[7]), U12.2G9 (LOGIC_DVDD[7]), U12.2H8 (LOGIC_DVDD[7]), U12.2H9 (LOGIC_DVDD[7]), U12.2J9 (LOGIC_MEM_DVDD[2])
- new net VDD_NPU_S0: C117.1, C118.1, C235.1, C307.1, C74.1, C75.1, C76.1, U12.2C7 (NPU_DVDD[5]), U12.2C8 (NPU_DVDD[5]), U12.2C9 (NPU_DVDD[5]), U12.2D7 (NPU_DVDD[5]), U12.2D8 (NPU_DVDD[5])
- new net Vdet_USB_{SOC}: U12.1AE1 (SAI4_SDI_M2)
- new net WIFI_REG_ON_L: U12.1W22 (SAI0_MCLK_M1)
- new net WIFI_RESET_L: U12.1AA22 (SAI0_SDO0_M1)
- new net WIFI_WAKE_DEV_L: U12.1E22 (ETH_CLK1_25M_OUT_M1)
- new net WIFI_WAKE_HOST_L: U12.1E21 (ETH1_MCLK_M1)
- new net WIRELESS_ALERT_L: U12.1Y21 (SAI0_SCLK_M1)
- new net uSD_CLK: U12.1B21 (SDMMC0_CLK)
- new net uSD_CMD: U12.1A21 (SDMMC0_CMD)
- new net uSD_D0: U12.B24 (SDMMC0_D0)
- new net uSD_D1: U12.B25 (SDMMC0_D1)
- new net uSD_D2: U12.A23 (SDMMC0_D2)
- new net uSD_D3: U12.B23 (SDMMC0_D3)
- new net uSD_DET: U12.1U21 (SDMMC0_DETN)
- no-connect marks 0 -> 34
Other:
- removed sheet GPIO0
- removed sheet GPIO1
- removed sheet GPIO2
- removed sheet GPIO3
- removed sheet GPIO4
- removed sheet HDMI PHY
- removed sheet LPDDR PHY
- removed sheet MIPI PHY
- removed sheet RK3576 PCIe
- removed sheet RK3576 Power
- removed sheet RK3576 UFS
- removed sheet RK3576 USB2
- removed sheet RK3576 USB3 DP1.4
- removed sheet RK3576 eMMC
- removed sheet RK3576 uSD Card
- removed sheet SARADC
- note added: "ELECTROSTATIC-SENSITIVE DEVICE"
- note added: "HOT SURFACE"
- note removed: "https://github.com/as-jackson/RK3576-Development-Board/blob/main/RK3576-Schematics/rk3576-compute-module-ArmSoM-CM5-1V1_sch.pdf"

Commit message: Replace v2 with updated RK3576_SBCv2 (Copy) Oct 2
- Update 18 sheets to Oct 2 15:37 local versions
- Keep cleaned layout: exclude .history/, Resources/, *.bak, *.lck,
  project.kicad_dru, .hs_rules.json, lowercase dup placeholders
  (fixtures/power), empty orphans (digital, mechanical, output,
  USBC_MCU, eMMC_UFS)
- Preserve LICENSE, README.md, .gitignore
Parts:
- added R286, R287, R288, R289: 4.7k, PCM_Resistor_SMD_AKL:R_0402_1005Metric, symbol Device:R_Small
- C119, C121, C358, C359: footprint Capacitor_SMD:C_0402_1005Metric_Pad0.74x0.62mm_HandSolder -> Capacitor_SMD:C_0402_1005Metric
- R148: LCSC Part C105871 -> C137961; Mouser Part 603-RC0402FR-074K7L -> 603-RC0402FR-07510KL
- R18: LCSC Part C60491 -> C60490; Mouser Part 603-RC0402FR-07100KL -> 603-RC0402FR-0710KL
- R227, R231, R232, R259: LCSC Part C114765 -> C106231; Mouser Part 603-RC0402FR-0722RL -> 603-RC0402FR-070RL
- R229: LCSC Part C105871 -> C106231; Mouser Part 603-RC0402FR-074K7L -> 603-RC0402FR-070RL
- U12: LCSC Part (none) -> C42388007
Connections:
- net 40GPIOs_GPIO(3_D3)_I3C(1)_SCL-M2 is gone; now on net Vdet_USB_{MCU}: U12.B12 (VO_LCDC_D0)
- net SPI1_{MCU}_CS: now also R289.2
- net SPI1_{MCU}_SCK: now also R286.2
- net SPI1_{MCU}_SDI: now also R288.2
- net SPI1_{MCU}_SDO: now also R287.2
- net VCCA_1V8_S3: now also C129.1, U12.2A7 (VCCIO4_VCC)
- net VCC_3.3v_S0: no longer C129.1, U12.2A7 (VCCIO4_VCC)
- net VCC_3V3_S0: now also R286.1, R287.1, R288.1, R289.1
- net Vdet_USB_{MCU}: no longer U12.1C12 (VO_LCDC_D3)
- net I2C0_SDA_M0_MIPI_CAM2_TP: now reaches U12.1P23 (SPI2_MISO_M0)
- net I2C0_SCL_M0_MIPI_CAM2_TP: now reaches U12.1U22 (AUPLL_CLK_IN_M1)
- net 40GPIOs_GPIO(3_A0)_UART(3)_RX-M1 renamed MIPI_DPHY_CSI_CAM2_RST_H
- net 40GPIOs_GPIO(3_A1)_UART(3)_RX-M1 renamed MIPI_DPHY_CSI_CAM2_PDN_H
- net 40GPIOs_GPIO(3_B2)_I2C(8)_SDA-M3 renamed I2C8_SDA_M3_RTC_EEPROM
- net 40GPIOs_GPIO(3_B3)_I2C(8)_SCL-M3 renamed I2C8_SCL_M3_RTC_EEPROM
- net 40GPIOs_GPIO(3_C2)_I2C(5)_SCL-M3 renamed 40GPIOs_GPIO(3_C2)_I2C(9)_SCL-M3
- net 40GPIOs_GPIO(3_C4)_I2C(9)_SCL-M3 renamed 40GPIOs_GPIO(3_C4)_I2C(5)_SCL-M3
- net 40GPIOs_GPIO(3_D1)_I3C(1)_SDA_PU-M2 renamed CAM2_CLK2_OUT_M0_1V8
- net 40GPIOs_GPIO(3_D2)_I3C(1)_SDA-M2 renamed MIPI_DPHY_CSI_CAM1_PDN_H
- net I2C0_SCL_M1_TP_Wireless: no longer names the net of U12.1V24 (I2C0_SDA_M1)
- net I2C0_SDA_M1_TP_Wireless: no longer names the net of U12.AB28 (I2C0_SCL_M1)
- net I2C2_SCL_M0_CC_RTC_EEPROM renamed I2C2_SCL_M0_USB_Wireless
- net I2C2_SDA_M0_CC_RTC_EEPROM renamed I2C2_SDA_M0_USB_Wireless
- new net CAM1_CLK1_OUT_M0_1V8: U12.1C12 (VO_LCDC_D3)
- no-connect marks 34 -> 36
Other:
- moved on the sheet: C137, C138, C139, C140, C141, C142, C145, C146, C151, R227, R231, R232
